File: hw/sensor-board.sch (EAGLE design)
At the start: 49 parts, among them U1 LT1762EMS8-3.3PBF, U2 ULN2003LVPWR, U3 ULN2003LVPWR, U4 PCA9685PW, U5 AT42QT1070-SSU, X1 MOLEX-501953-0407, X2 MOLEX-501953-0407

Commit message: Fix sourcing info for components.
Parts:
- C1: device rcl:C-EUC0603K -> rcl:C-EUC0805K; ELEMENT14_URL http://sg.element14.com/jsp/search/productdetail.jsp?sku=1833876 -> http://sg.element14.com/jsp/search/productdetail.jsp?sku=1833812; MFR_PART 06031C103JAT2A -> 0805ZD106KAT2A
- C13: value 0.01uF 16V -> 0.01uF 25V; ELEMENT14_URL http://sg.element14.com/jsp/search/productdetail.jsp?sku=87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 -> http://sg.element14.com/jsp/search/productdetail.jsp?sku=16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; MFR_PART C0402C103J4RACTU -> C0402C103J3RACTU
- C14, C15, C16, C17, C18, C19, C20, C21, C22, C23, C24: ELEMENT14_URL http://sg.element14.com/jsp/search/productdetail.jsp?sku=87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 -> http://sg.element14.com/jsp/search/productdetail.jsp?sku=16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; MFR_PART C0402C103J4RACTU -> C0402C103J3RACTU
- C2: value 0.01uF 100V -> 0.01uF 25V; ELEMENT14_URL http://sg.element14.com/jsp/search/productdetail.jsp?sku=18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 -> http://sg.element14.com/jsp/search/productdetail.jsp?sku=16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; MFR_PART 06031C103JAT2A -> C0402C103J3RACTU
- C3: device rcl:C-EUC0402K -> rcl:C-EUC0603K; ELEMENT14_URL http://sg.element14.com/jsp/search/productdetail.jsp?sku=18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 -> http://sg.element14.com/jsp/search/productdetail.jsp?sku=21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; MFR_PART 06031C103JAT2A -> C1608X7R1C105K080AC
- C4: value 0.01uF 100V -> 0.1uF 100V; ELEMENT14_URL http://sg.element14.com/jsp/search/productdetail.jsp?sku=1833876 -> http://sg.element14.com/jsp/search/productdetail.jsp?sku=1833861; MFR_PART 06031C103JAT2A -> 0402YC104KAT2A
- R1: MFR_PART PCF0402PR-4K7BT1 -> PCF0402PR-4K7BT1
- R10, R11, R12, R13, R14, R15, R16, R17, R18, R19, R20, R9: ELEMENT14_URL http://sg.element14.com/jsp/search/productdetail.jsp?sku=17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 -> http://sg.element14.com/jsp/search/productdetail.jsp?sku=18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; MFR_PART CRCW060368R0FKEAHP -> ERJP03F62R0V

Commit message: Create option to share LDO between sensor boards.
This is done to reduce the BOM. If necessary, the voltage regulator can
be installed later on as the land pattern stays.

Label connector signals.

Adjust some silkscreen positions.
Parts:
- added PWR: (no value), pinhead:PINHD-1X2
- renumbered VDD to 5V
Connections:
- net GND: now also PWR.2, X1.5, X1.6, X2.5, X2.6
- net VDD_3_3: now also PWR.1
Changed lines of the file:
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@@
 <part name="X1" library="connector" deviceset="MOLEX-501953-0407" device=""/>
 <part name="TP1" library="testpad" deviceset="TP" device="B1,27"/>
-<part name="VDD" library="testpad" deviceset="TP" device="B1,27"/>
+<part name="5V" library="testpad" deviceset="TP" device="B1,27"/>
 <part name="TP3" library="testpad" deviceset="TP" device="B1,27"/>
 <part name="GND" library="testpad" deviceset="TP" device="B1,27"/>
@@
 <part name="A1" library="testpad" deviceset="TP" device="B1,27"/>
 <part name="U5" library="touch_ctl" deviceset="AT42QT1070" device="-SSU"/>
+<part name="PWR" library="pinhead" deviceset="PINHD-1X2" device=""/>
 </parts>
 <sheets>
@@
 <instance part="X1" gate="G$1" x="38.1" y="220.98"/>
 <instance part="TP1" gate="G$1" x="58.42" y="12.7" rot="R180"/>
-<instance part="VDD" gate="G$1" x="78.74" y="12.7" rot="R180"/>
+<instance part="5V" gate="G$1" x="78.74" y="12.7" rot="R180"/>
 <instance part="TP3" gate="G$1" x="58.42" y="-12.7" rot="R180"/>
 <instance part="GND" gate="G$1" x="78.74" y="-12.7" rot="R180"/>
@@
 <instance part="A1" gate="G$1" x="78.74" y="0" rot="R180"/>
 <instance part="U5" gate="G$1" x="284.48" y="226.06"/>
+<instance part="PWR" gate="G$1" x="238.76" y="264.16" rot="R90"/>
 </instances>
 <busses>
@@
 <wire x1="165.1" y1="259.08" x2="220.98" y2="259.08" width="0.1524" layer="91"/>
 <wire x1="220.98" y1="259.08" x2="220.98" y2="243.84" width="0.1524" layer="91"/>
-<wire x1="220.98" y1="243.84" x2="264.16" y2="243.84" width="0.1524" layer="91"/>
+<wire x1="220.98" y1="243.84" x2="236.22" y2="243.84" width="0.1524" layer="91"/>
 <pinref part="C4" gate="G$1" pin="1"/>
 <pinref part="C1" gate="G$1" pin="1"/>
 <pinref part="U1" gate="A" pin="OUT"/>
+<wire x1="236.22" y1="243.84" x2="264.16" y2="243.84" width="0.1524" layer="91"/>
 <wire x1="210.82" y1="241.3" x2="213.36" y2="241.3" width="0.1524" layer="91"/>
 <wire x1="213.36" y1="241.3" x2="213.36" y2="238.76" width="0.1524" layer="91"/>
@@
 <pinref part="C2" gate="G$1" pin="2"/>
 <wire x1="213.36" y1="243.84" x2="213.36" y2="241.3" width="0.1524" layer="91"/>
+<pinref part="PWR" gate="G$1" pin="1"/>
+<wire x1="236.22" y1="261.62" x2="236.22" y2="243.84" width="0.1524" layer="91"/>
+<junction x="236.22" y="243.84"/>
 </segment>
 </net>
@@
 <pinref part="TP1" gate="G$1" pin="TP"/>
 <wire x1="58.42" y1="15.24" x2="58.42" y2="17.78" width="0.1524" layer="91"/>
-<pinref part="VDD" gate="G$1" pin="TP"/>
+<pinref part="5V" gate="G$1" pin="TP"/>
 <wire x1="58.42" y1="17.78" x2="78.74" y2="17.78" width="0.1524" layer="91"/>
 <wire x1="78.74" y1="17.78" x2="78.74" y2="15.24" width="0.1524" layer="91"/>
@@
 <junction x="111.76" y="218.44"/>
 <wire x1="264.16" y1="231.14" x2="256.54" y2="231.14" width="0.1524" layer="91"/>
-<wire x1="256.54" y1="231.14" x2="213.36" y2="231.14" width="0.1524" layer="91"/>
+<wire x1="256.54" y1="231.14" x2="238.76" y2="231.14" width="0.1524" layer="91"/>
 <pinref part="C4" gate="G$1" pin="2"/>
 <junction x="256.54" y="231.14"/>
-<wire x1="45.72" y1="228.6" x2="111.76" y2="228.6" width="0.1524" layer="91"/>
+<wire x1="238.76" y1="231.14" x2="213.36" y2="231.14" width="0.1524" layer="91"/>
+<wire x1="45.72" y1="228.6" x2="50.8" y2="228.6" width="0.1524" layer="91"/>
+<wire x1="50.8" y1="228.6" x2="111.76" y2="228.6" width="0.1524" layer="91"/>
 <wire x1="111.76" y1="228.6" x2="111.76" y2="218.44" width="0.1524" layer="91"/>
 <pinref part="C3" gate="G$1" pin="2"/>
@@
 <wire x1="264.16" y1="236.22" x2="264.16" y2="231.14" width="0.1524" layer="91"/>
 <junction x="264.16" y="231.14"/>
+<pinref part="X1" gate="G$1" pin="6"/>
+<wire x1="45.72" y1="208.28" x2="50.8" y2="208.28" width="0.1524" layer="91"/>
+<wire x1="50.8" y1="208.28" x2="50.8" y2="213.36" width="0.1524" layer="91"/>
+<pinref part="X1" gate="G$1" pin="5"/>
+<wire x1="50.8" y1="213.36" x2="50.8" y2="228.6" width="0.1524" layer="91"/>
+<wire x1="45.72" y1="213.36" x2="50.8" y2="213.36" width="0.1524" layer="91"/>
+<junction x="50.8" y="213.36"/>
+<junction x="50.8" y="228.6"/>
+<pinref part="PWR" gate="G$1" pin="2"/>
+<wire x1="238.76" y1="261.62" x2="238.76" y2="231.14" width="0.1524" layer="91"/>
+<junction x="238.76" y="231.14"/>
 </segment>
 <segment>
@@
 <wire x1="490.22" y1="96.52" x2="490.22" y2="99.06" width="0.1524" layer="91"/>
 <pinref part="X2" gate="G$1" pin="2"/>
-<wire x1="45.72" y1="71.12" x2="93.98" y2="71.12" width="0.1524" layer="91"/>
+<wire x1="45.72" y1="71.12" x2="50.8" y2="71.12" width="0.1524" layer="91"/>
+<wire x1="50.8" y1="71.12" x2="93.98" y2="71.12" width="0.1524" layer="91"/>
 <wire x1="93.98" y1="71.12" x2="93.98" y2="99.06" width="0.1524" layer="91"/>
 <junction x="231.14" y="99.06"/>
@@
 <wire x1="106.68" y1="17.78" x2="106.68" y2="10.16" width="0.1524" layer="91"/>
 <junction x="106.68" y="10.16"/>
+<pinref part="X2" gate="G$1" pin="6"/>
+<wire x1="45.72" y1="50.8" x2="50.8" y2="50.8" width="0.1524" layer="91"/>
+<wire x1="50.8" y1="50.8" x2="50.8" y2="55.88" width="0.1524" layer="91"/>
+<junction x="50.8" y="71.12"/>
+<pinref part="X2" gate="G$1" pin="5"/>
+<wire x1="50.8" y1="55.88" x2="50.8" y2="71.12" width="0.1524" layer="91"/>
+<wire x1="45.72" y1="55.88" x2="50.8" y2="55.88" width="0.1524" layer="91"/>
+<junction x="50.8" y="55.88"/>
 </segment>
 </net>

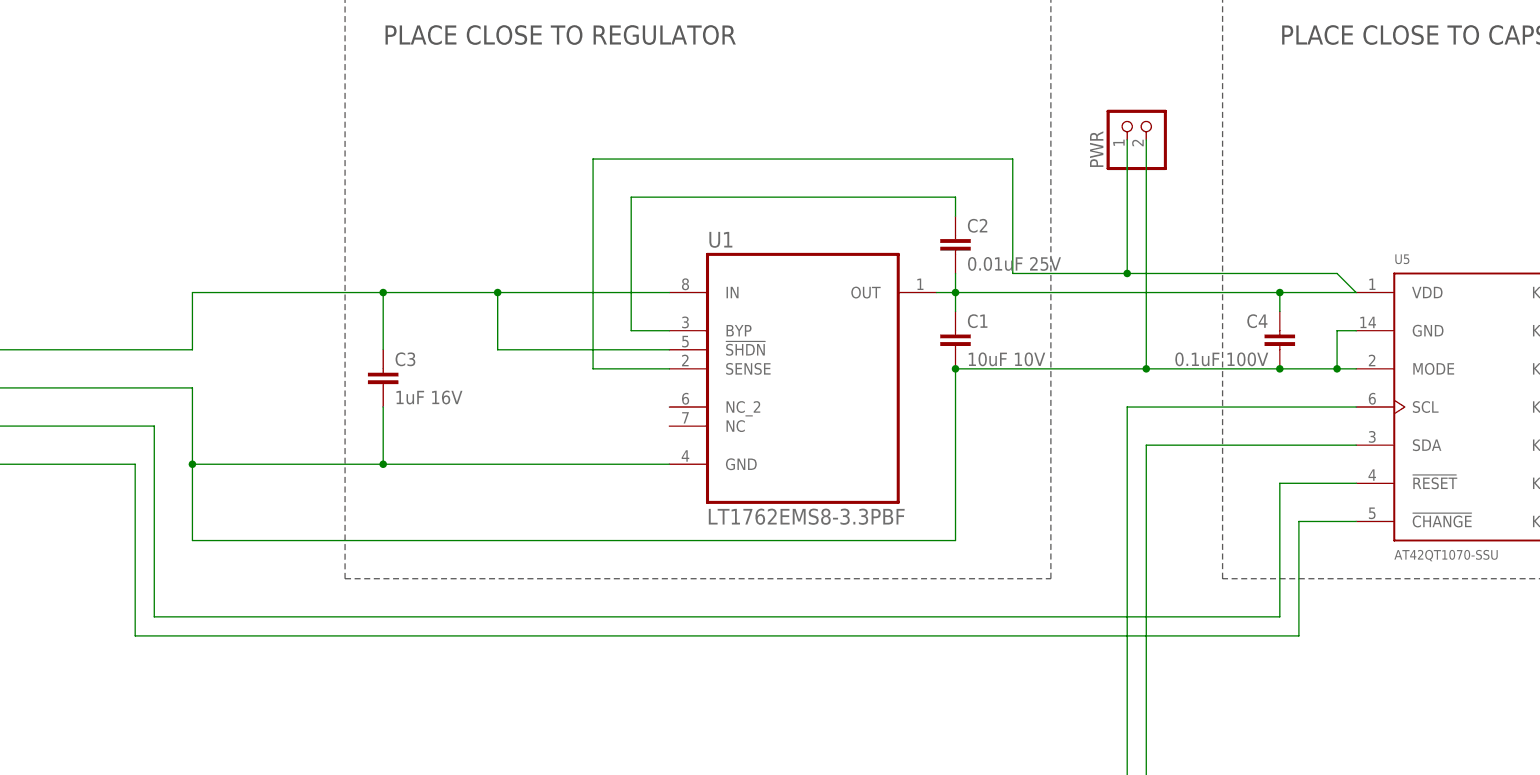
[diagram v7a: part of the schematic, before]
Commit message: Add pullup to capsense change line.
Capsense schematic and layout checked wrt datasheet.
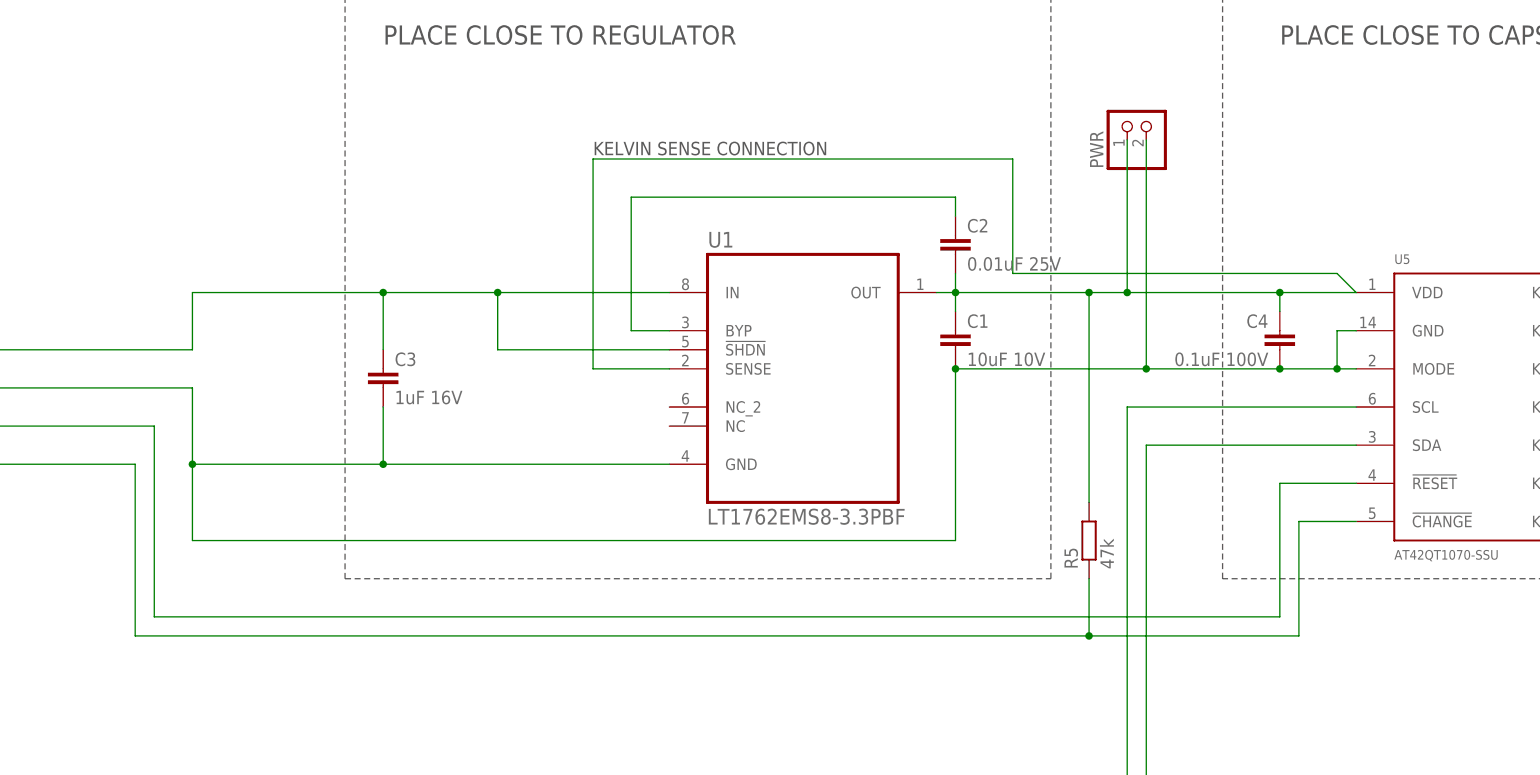
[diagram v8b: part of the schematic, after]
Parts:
- added R5: 47k, myrcl:R-EU_NKR0603
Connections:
- net !CAPSENSE_CHG!: now also R5.1
- net VDD_3_3: now also R5.2
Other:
- note added: "KELVIN SENSE CONNECTION"
